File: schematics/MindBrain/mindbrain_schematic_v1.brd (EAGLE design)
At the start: 92.4 x 49.5 mm, 49 parts, among them CON1 POWER, IC1 TL084P, IC2 TL084P

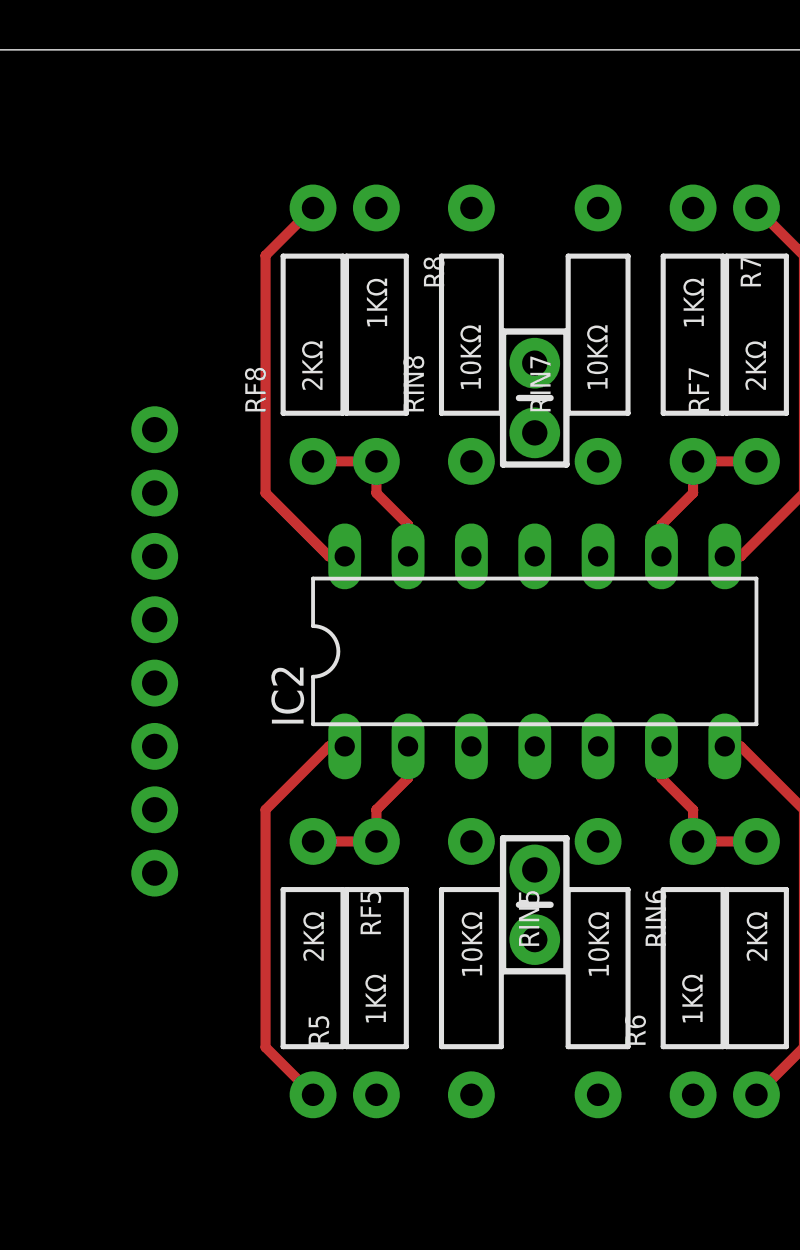
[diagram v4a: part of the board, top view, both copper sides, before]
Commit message: layed out input traces for channels 5, 6, 7, 8
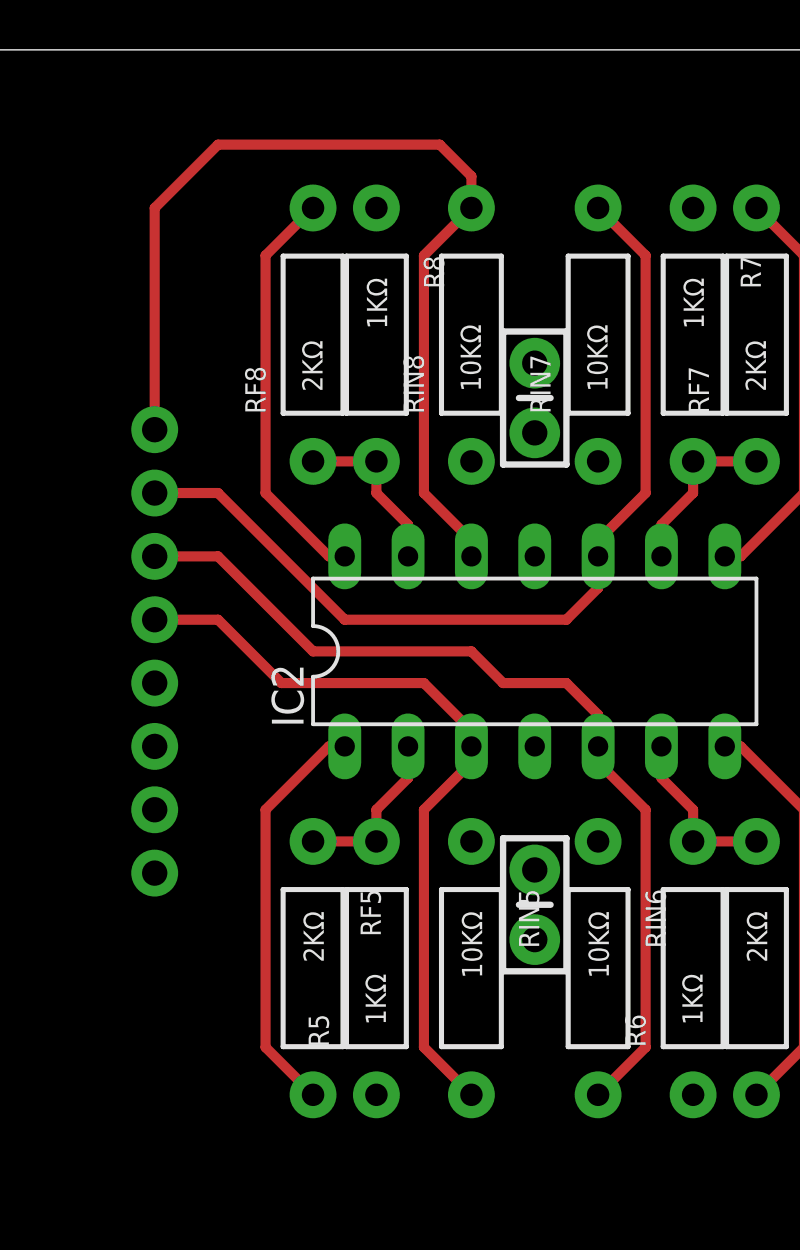
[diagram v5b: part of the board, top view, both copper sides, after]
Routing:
- net N$22: track 0.00 -> 40.0 mm
- net N$19: track 0.00 -> 37.2 mm
- net N$16: track 0.00 -> 37.2 mm
- net N$13: track 0.00 -> 30.7 mm
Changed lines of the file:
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@@
 <contactref element="RIN1" pad="P$2"/>
 <contactref element="IC1" pad="3"/>
-<wire x1="26.67" y1="16.51" x2="64.77" y2="21.59" width="0" layer="19" extent="1-1"/>
 <wire x1="64.77" y1="7.62" x2="62.865" y2="9.525" width="0.4064" layer="1"/>
 <wire x1="62.865" y1="9.525" x2="62.865" y2="19.05" width="0.4064" layer="1"/>
 <wire x1="62.865" y1="19.05" x2="64.77" y2="20.955" width="0.4064" layer="1"/>
 <wire x1="64.77" y1="20.955" x2="64.77" y2="21.59" width="0.4064" layer="1"/>
+<wire x1="26.67" y1="16.51" x2="26.67" y2="8.89" width="0" layer="19" extent="1-16"/>
+<wire x1="26.67" y1="8.89" x2="29.845" y2="5.715" width="0" layer="19" extent="1-16"/>
+<wire x1="29.845" y1="5.715" x2="62.865" y2="5.715" width="0" layer="19" extent="1-16"/>
+<wire x1="62.865" y1="5.715" x2="64.77" y2="7.62" width="0" layer="19" extent="1-16"/>
 </signal>
 <signal name="GND">
@@
 <contactref element="RIN2" pad="P$2"/>
 <contactref element="IC1" pad="5"/>
-<wire x1="26.67" y1="19.05" x2="69.85" y2="21.59" width="0" layer="19" extent="1-1"/>
 <wire x1="69.85" y1="7.62" x2="71.755" y2="9.525" width="0.4064" layer="1"/>
 <wire x1="71.755" y1="9.525" x2="71.755" y2="19.05" width="0.4064" layer="1"/>
 <wire x1="71.755" y1="19.05" x2="69.85" y2="20.955" width="0.4064" layer="1"/>
 <wire x1="69.85" y1="20.955" x2="69.85" y2="21.59" width="0.4064" layer="1"/>
+<wire x1="26.67" y1="19.05" x2="69.85" y2="20.955" width="0" layer="19" extent="1-1"/>
 </signal>
 <signal name="N$5">
@@
 <contactref element="RIN5" pad="P$2"/>
 <contactref element="IC2" pad="3"/>
-<wire x1="26.67" y1="26.67" x2="39.37" y2="21.59" width="0" layer="19" extent="1-1"/>
-<wire x1="39.37" y1="7.62" x2="39.37" y2="21.59" width="0" layer="19" extent="1-1"/>
+<wire x1="39.37" y1="7.62" x2="37.465" y2="9.525" width="0.4064" layer="1"/>
+<wire x1="37.465" y1="9.525" x2="37.465" y2="19.05" width="0.4064" layer="1"/>
+<wire x1="37.465" y1="19.05" x2="39.37" y2="20.955" width="0.4064" layer="1"/>
+<wire x1="39.37" y1="20.955" x2="39.37" y2="21.59" width="0.4064" layer="1"/>
+<wire x1="26.67" y1="26.67" x2="29.21" y2="26.67" width="0.4064" layer="1"/>
+<wire x1="29.21" y1="26.67" x2="31.75" y2="24.13" width="0.4064" layer="1"/>
+<wire x1="31.75" y1="24.13" x2="37.465" y2="24.13" width="0.4064" layer="1"/>
+<wire x1="37.465" y1="24.13" x2="39.37" y2="22.225" width="0.4064" layer="1"/>
+<wire x1="39.37" y1="22.225" x2="39.37" y2="21.59" width="0.4064" layer="1"/>
 </signal>
 <signal name="N$14">
@@
 <contactref element="RIN6" pad="P$2"/>
 <contactref element="IC2" pad="5"/>
-<wire x1="44.45" y1="7.62" x2="44.45" y2="21.59" width="0" layer="19" extent="1-1"/>
-<wire x1="26.67" y1="29.21" x2="44.45" y2="21.59" width="0" layer="19" extent="1-1"/>
+<wire x1="44.45" y1="7.62" x2="46.355" y2="9.525" width="0.4064" layer="1"/>
+<wire x1="46.355" y1="9.525" x2="46.355" y2="19.05" width="0.4064" layer="1"/>
+<wire x1="46.355" y1="19.05" x2="44.45" y2="20.955" width="0.4064" layer="1"/>
+<wire x1="44.45" y1="20.955" x2="44.45" y2="21.59" width="0.4064" layer="1"/>
+<wire x1="26.67" y1="29.21" x2="29.21" y2="29.21" width="0.4064" layer="1"/>
+<wire x1="29.21" y1="29.21" x2="33.02" y2="25.4" width="0.4064" layer="1"/>
+<wire x1="33.02" y1="25.4" x2="39.37" y2="25.4" width="0.4064" layer="1"/>
+<wire x1="39.37" y1="25.4" x2="40.64" y2="24.13" width="0.4064" layer="1"/>
+<wire x1="40.64" y1="24.13" x2="43.18" y2="24.13" width="0.4064" layer="1"/>
+<wire x1="43.18" y1="24.13" x2="44.45" y2="22.86" width="0.4064" layer="1"/>
+<wire x1="44.45" y1="22.86" x2="44.45" y2="21.59" width="0.4064" layer="1"/>
 </signal>
 <signal name="N$17">
@@
 <contactref element="RIN7" pad="P$2"/>
 <contactref element="IC2" pad="10"/>
-<wire x1="44.45" y1="29.21" x2="44.45" y2="43.18" width="0" layer="19" extent="1-1"/>
-<wire x1="26.67" y1="31.75" x2="44.45" y2="29.21" width="0" layer="19" extent="1-1"/>
+<wire x1="44.45" y1="43.18" x2="46.355" y2="41.275" width="0.4064" layer="1"/>
+<wire x1="46.355" y1="41.275" x2="46.355" y2="31.75" width="0.4064" layer="1"/>
+<wire x1="46.355" y1="31.75" x2="44.45" y2="29.845" width="0.4064" layer="1"/>
+<wire x1="44.45" y1="29.845" x2="44.45" y2="29.21" width="0.4064" layer="1"/>
+<wire x1="26.67" y1="31.75" x2="29.21" y2="31.75" width="0.4064" layer="1"/>
+<wire x1="29.21" y1="31.75" x2="34.29" y2="26.67" width="0.4064" layer="1"/>
+<wire x1="34.29" y1="26.67" x2="43.18" y2="26.67" width="0.4064" layer="1"/>
+<wire x1="43.18" y1="26.67" x2="44.45" y2="27.94" width="0.4064" layer="1"/>
+<wire x1="44.45" y1="27.94" x2="44.45" y2="29.21" width="0.4064" layer="1"/>
 </signal>
 <signal name="N$20">
@@
 <contactref element="RIN8" pad="P$2"/>
 <contactref element="IC2" pad="12"/>
-<wire x1="39.37" y1="29.21" x2="39.37" y2="43.18" width="0" layer="19" extent="1-1"/>
-<wire x1="26.67" y1="34.29" x2="39.37" y2="29.21" width="0" layer="19" extent="1-1"/>
+<wire x1="39.37" y1="43.18" x2="37.465" y2="41.275" width="0.4064" layer="1"/>
+<wire x1="37.465" y1="41.275" x2="37.465" y2="31.75" width="0.4064" layer="1"/>
+<wire x1="37.465" y1="31.75" x2="39.37" y2="29.845" width="0.4064" layer="1"/>
+<wire x1="39.37" y1="29.845" x2="39.37" y2="29.21" width="0.4064" layer="1"/>
+<wire x1="26.67" y1="34.29" x2="26.67" y2="43.18" width="0.4064" layer="1"/>
+<wire x1="26.67" y1="43.18" x2="29.21" y2="45.72" width="0.4064" layer="1"/>
+<wire x1="29.21" y1="45.72" x2="38.1" y2="45.72" width="0.4064" layer="1"/>
+<wire x1="38.1" y1="45.72" x2="39.37" y2="44.45" width="0.4064" layer="1"/>
+<wire x1="39.37" y1="44.45" x2="39.37" y2="43.18" width="0.4064" layer="1"/>
 </signal>
 <signal name="N$23">

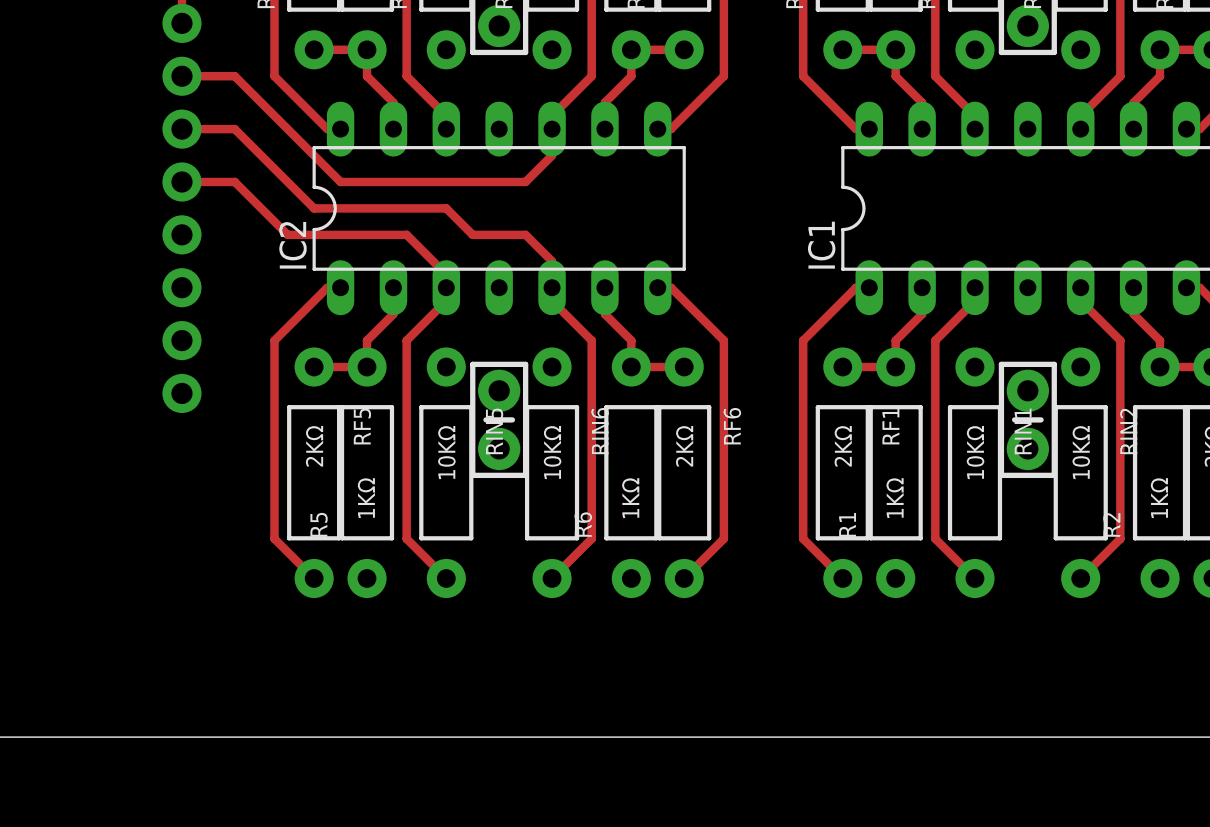
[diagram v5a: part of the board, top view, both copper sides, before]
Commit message: layed out all input traces
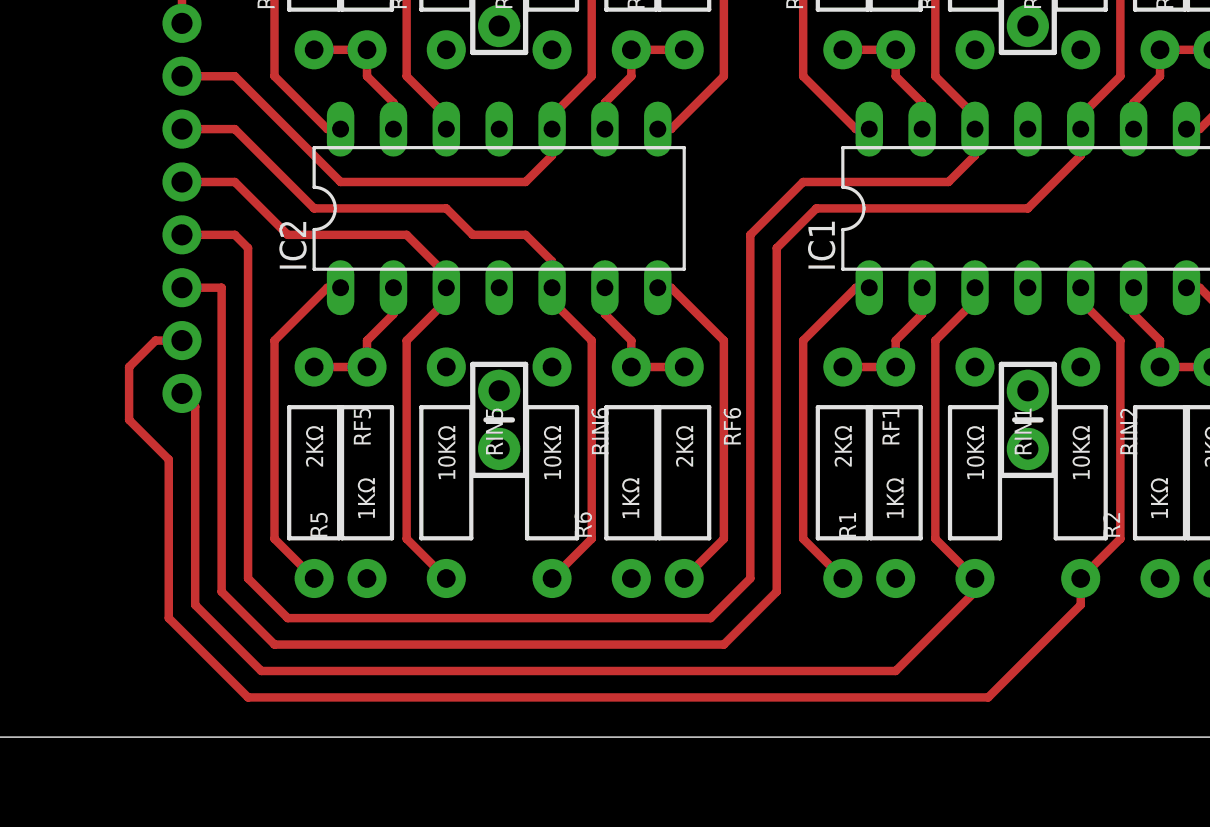
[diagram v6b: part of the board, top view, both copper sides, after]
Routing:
- net N$7: track 15.5 -> 95.1 mm
- net N$10: track 15.5 -> 90.7 mm
- net N$4: track 15.5 -> 80.0 mm
- net N$1: track 15.5 -> 67.0 mm
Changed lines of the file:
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@@
 <wire x1="62.865" y1="19.05" x2="64.77" y2="20.955" width="0.4064" layer="1"/>
 <wire x1="64.77" y1="20.955" x2="64.77" y2="21.59" width="0.4064" layer="1"/>
-<wire x1="26.67" y1="16.51" x2="26.67" y2="8.89" width="0" layer="19" extent="1-16"/>
-<wire x1="26.67" y1="8.89" x2="29.845" y2="5.715" width="0" layer="19" extent="1-16"/>
-<wire x1="29.845" y1="5.715" x2="62.865" y2="5.715" width="0" layer="19" extent="1-16"/>
-<wire x1="62.865" y1="5.715" x2="64.77" y2="7.62" width="0" layer="19" extent="1-16"/>
+<wire x1="26.67" y1="16.51" x2="27.305" y2="15.875" width="0.4064" layer="1"/>
+<wire x1="27.305" y1="15.875" x2="27.305" y2="6.35" width="0.4064" layer="1"/>
+<wire x1="27.305" y1="6.35" x2="30.48" y2="3.175" width="0.4064" layer="1"/>
+<wire x1="30.48" y1="3.175" x2="60.96" y2="3.175" width="0.4064" layer="1"/>
+<wire x1="60.96" y1="3.175" x2="64.77" y2="6.985" width="0.4064" layer="1"/>
+<wire x1="64.77" y1="6.985" x2="64.77" y2="7.62" width="0.4064" layer="1"/>
 </signal>
 <signal name="GND">
@@
 <wire x1="71.755" y1="19.05" x2="69.85" y2="20.955" width="0.4064" layer="1"/>
 <wire x1="69.85" y1="20.955" x2="69.85" y2="21.59" width="0.4064" layer="1"/>
-<wire x1="26.67" y1="19.05" x2="69.85" y2="20.955" width="0" layer="19" extent="1-1"/>
+<wire x1="26.67" y1="19.05" x2="25.4" y2="19.05" width="0.4064" layer="1"/>
+<wire x1="25.4" y1="19.05" x2="24.13" y2="17.78" width="0.4064" layer="1"/>
+<wire x1="24.13" y1="17.78" x2="24.13" y2="15.24" width="0.4064" layer="1"/>
+<wire x1="24.13" y1="15.24" x2="26.035" y2="13.335" width="0.4064" layer="1"/>
+<wire x1="26.035" y1="13.335" x2="26.035" y2="5.715" width="0.4064" layer="1"/>
+<wire x1="26.035" y1="5.715" x2="29.845" y2="1.905" width="0.4064" layer="1"/>
+<wire x1="29.845" y1="1.905" x2="65.405" y2="1.905" width="0.4064" layer="1"/>
+<wire x1="65.405" y1="1.905" x2="69.85" y2="6.35" width="0.4064" layer="1"/>
+<wire x1="69.85" y1="6.35" x2="69.85" y2="7.62" width="0.4064" layer="1"/>
 </signal>
 <signal name="N$5">
@@
 <contactref element="RIN3" pad="P$2"/>
 <contactref element="IC1" pad="10"/>
-<wire x1="26.67" y1="21.59" x2="69.85" y2="29.21" width="0" layer="19" extent="1-1"/>
 <wire x1="69.85" y1="43.18" x2="71.755" y2="41.275" width="0.4064" layer="1"/>
 <wire x1="71.755" y1="41.275" x2="71.755" y2="31.75" width="0.4064" layer="1"/>
 <wire x1="71.755" y1="31.75" x2="69.85" y2="29.845" width="0.4064" layer="1"/>
 <wire x1="69.85" y1="29.845" x2="69.85" y2="29.21" width="0.4064" layer="1"/>
+<wire x1="26.67" y1="21.59" x2="28.575" y2="21.59" width="0.4064" layer="1"/>
+<wire x1="28.575" y1="21.59" x2="28.575" y2="6.985" width="0.4064" layer="1"/>
+<wire x1="28.575" y1="6.985" x2="31.115" y2="4.445" width="0.4064" layer="1"/>
+<wire x1="31.115" y1="4.445" x2="52.705" y2="4.445" width="0.4064" layer="1"/>
+<wire x1="52.705" y1="4.445" x2="55.245" y2="6.985" width="0.4064" layer="1"/>
+<wire x1="55.245" y1="6.985" x2="55.245" y2="23.495" width="0.4064" layer="1"/>
+<wire x1="55.245" y1="23.495" x2="57.15" y2="25.4" width="0.4064" layer="1"/>
+<wire x1="57.15" y1="25.4" x2="67.31" y2="25.4" width="0.4064" layer="1"/>
+<wire x1="67.31" y1="25.4" x2="69.85" y2="27.94" width="0.4064" layer="1"/>
+<wire x1="69.85" y1="27.94" x2="69.85" y2="29.21" width="0.4064" layer="1"/>
 </signal>
 <signal name="N$8">
@@
 <contactref element="RIN4" pad="P$2"/>
 <contactref element="IC1" pad="12"/>
-<wire x1="26.67" y1="24.13" x2="64.77" y2="29.21" width="0" layer="19" extent="1-1"/>
 <wire x1="64.77" y1="43.18" x2="62.865" y2="41.275" width="0.4064" layer="1"/>
 <wire x1="62.865" y1="41.275" x2="62.865" y2="31.75" width="0.4064" layer="1"/>
 <wire x1="62.865" y1="31.75" x2="64.77" y2="29.845" width="0.4064" layer="1"/>
 <wire x1="64.77" y1="29.845" x2="64.77" y2="29.21" width="0.4064" layer="1"/>
+<wire x1="26.67" y1="24.13" x2="29.21" y2="24.13" width="0.4064" layer="1"/>
+<wire x1="29.21" y1="24.13" x2="29.845" y2="23.495" width="0.4064" layer="1"/>
+<wire x1="29.845" y1="23.495" x2="29.845" y2="7.62" width="0.4064" layer="1"/>
+<wire x1="29.845" y1="7.62" x2="31.75" y2="5.715" width="0.4064" layer="1"/>
+<wire x1="31.75" y1="5.715" x2="52.07" y2="5.715" width="0.4064" layer="1"/>
+<wire x1="52.07" y1="5.715" x2="53.975" y2="7.62" width="0.4064" layer="1"/>
+<wire x1="53.975" y1="7.62" x2="53.975" y2="24.13" width="0.4064" layer="1"/>
+<wire x1="53.975" y1="24.13" x2="56.515" y2="26.67" width="0.4064" layer="1"/>
+<wire x1="56.515" y1="26.67" x2="63.5" y2="26.67" width="0.4064" layer="1"/>
+<wire x1="63.5" y1="26.67" x2="64.77" y2="27.94" width="0.4064" layer="1"/>
+<wire x1="64.77" y1="27.94" x2="64.77" y2="29.21" width="0.4064" layer="1"/>
 </signal>
 <signal name="N$11">
